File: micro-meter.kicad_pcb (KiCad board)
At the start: 2 copper layers, 50 x 50 mm, 93 parts, among them J1 DC_IN, J10 5V_OUT, J11 LEDS_DATA, J2 SPI, J3 I2C / UART, J4 IN1, J5 IN2, J6 IN3, J7 IN4, J8 SWD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

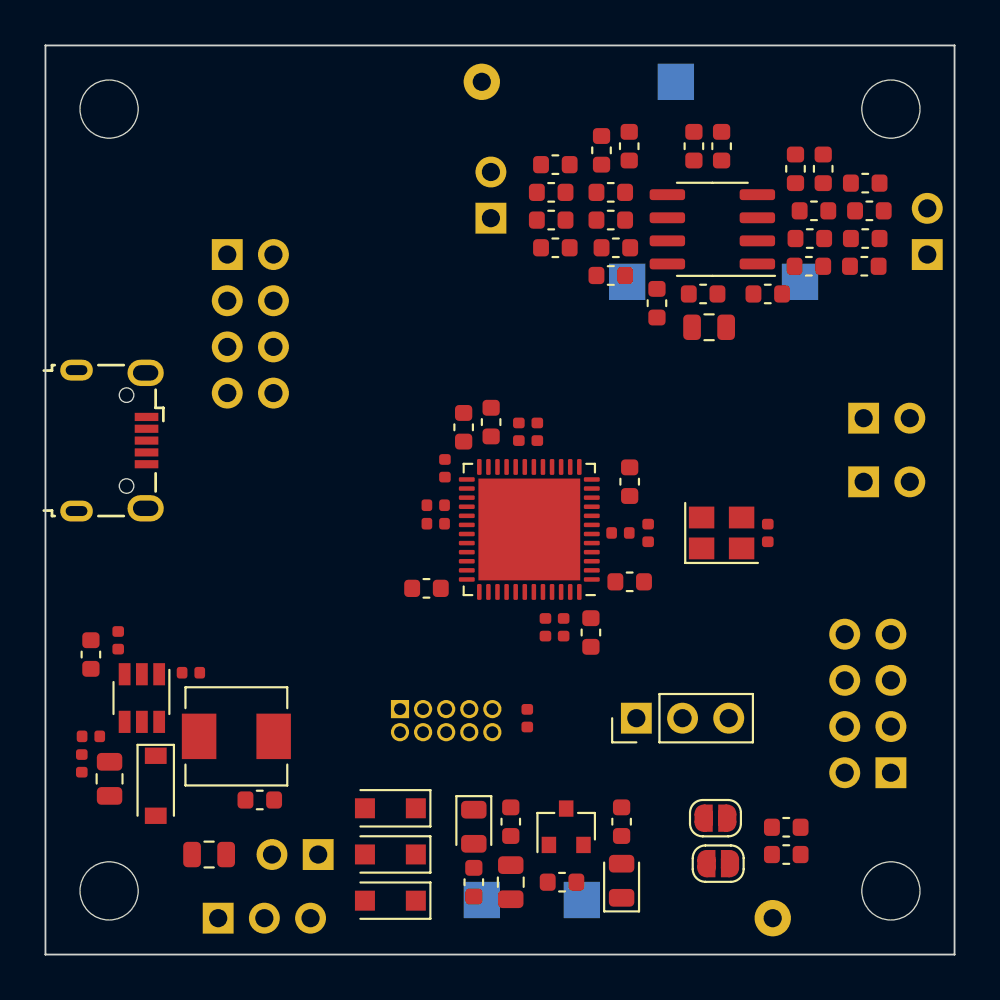
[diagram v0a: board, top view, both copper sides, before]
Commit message: Add inner layers and planes
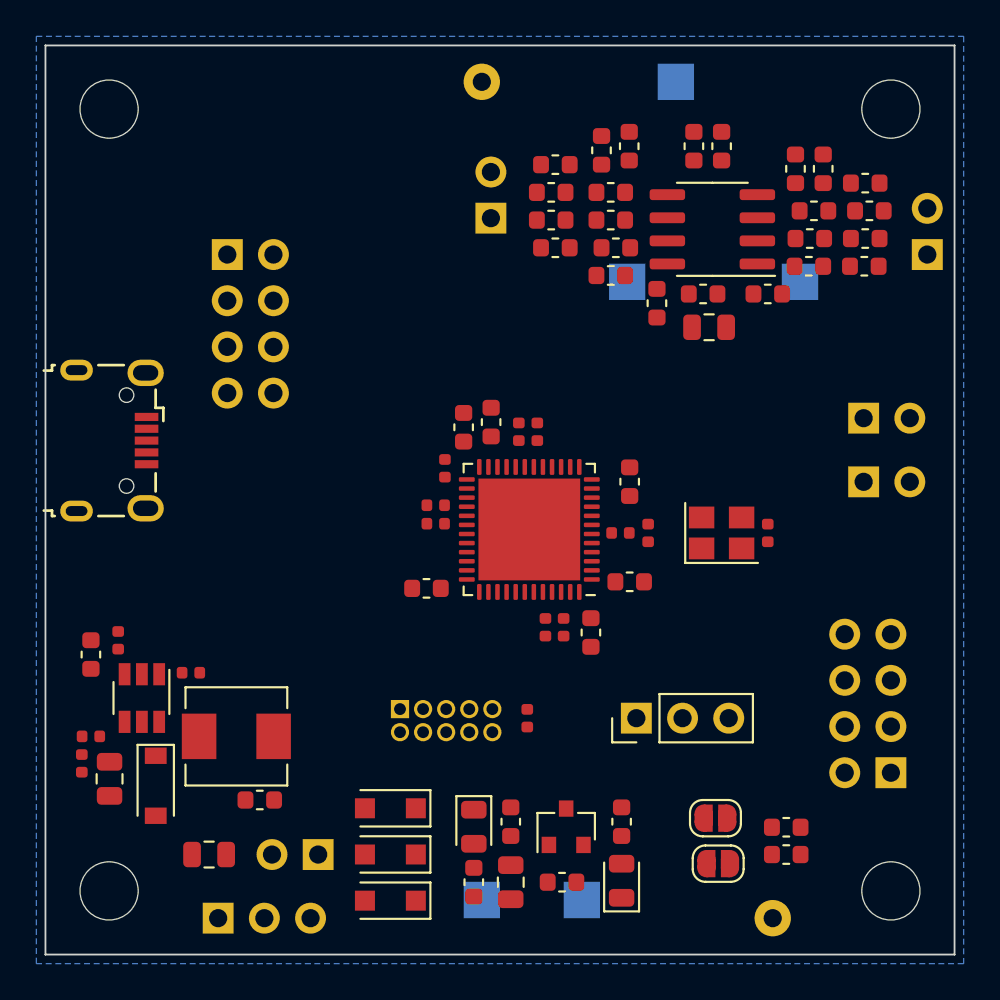
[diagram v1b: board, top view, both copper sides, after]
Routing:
- added copper zone on B.Cu, net +3V3
- added copper zone on In1.Cu, net GND
- added copper zone on In2.Cu, net GND
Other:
- copper layers 2 -> 4
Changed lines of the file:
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@@
   (layers
     (0 F.Cu signal)
+    (1 In1.Cu power)
+    (2 In2.Cu power)
     (31 B.Cu signal)
     (32 B.Adhes user)
@@
   (gr_line (start 70 170) (end 70 120) (layer Edge.Cuts) (width 0.1))
   (gr_line (start 120 170) (end 70 170) (layer Edge.Cuts) (width 0.1))
+  (zone (net 2) (net_name GND) (layer In1.Cu) (hatch edge 0.508)
+    (connect_pads (clearance 0.508))
+    (min_thickness 0.254)
+    (fill yes (arc_segments 32) (thermal_gap 0.508) (thermal_bridge_width 0.508))
+    (polygon
+      (pts
+        (xy 120.5 170.5) (xy 69.5 170.5) (xy 69.5 119.5) (xy 120.5 119.5)
+      )
+    )
+  )
+  (zone (net 2) (net_name GND) (layer In2.Cu) (hatch edge 0.508)
+    (connect_pads (clearance 0.508))
+    (min_thickness 0.254)
+    (fill yes (arc_segments 32) (thermal_gap 0.508) (thermal_bridge_width 0.508))
+    (polygon
+      (pts
+        (xy 120.5 170.5) (xy 69.5 170.5) (xy 69.5 119.5) (xy 120.5 119.5)
+      )
+    )
+  )
+  (zone (net 4) (net_name +3V3) (layer B.Cu) (hatch edge 0.508)
+    (connect_pads (clearance 0.508))
+    (min_thickness 0.254)
+    (fill yes (arc_segments 32) (thermal_gap 0.508) (thermal_bridge_width 0.508))
+    (polygon
+      (pts
+        (xy 120.5 170.5) (xy 69.5 170.5) (xy 69.5 119.5) (xy 120.5 119.5)
+      )
+    )
+  )
 )

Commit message: Add rounded corners
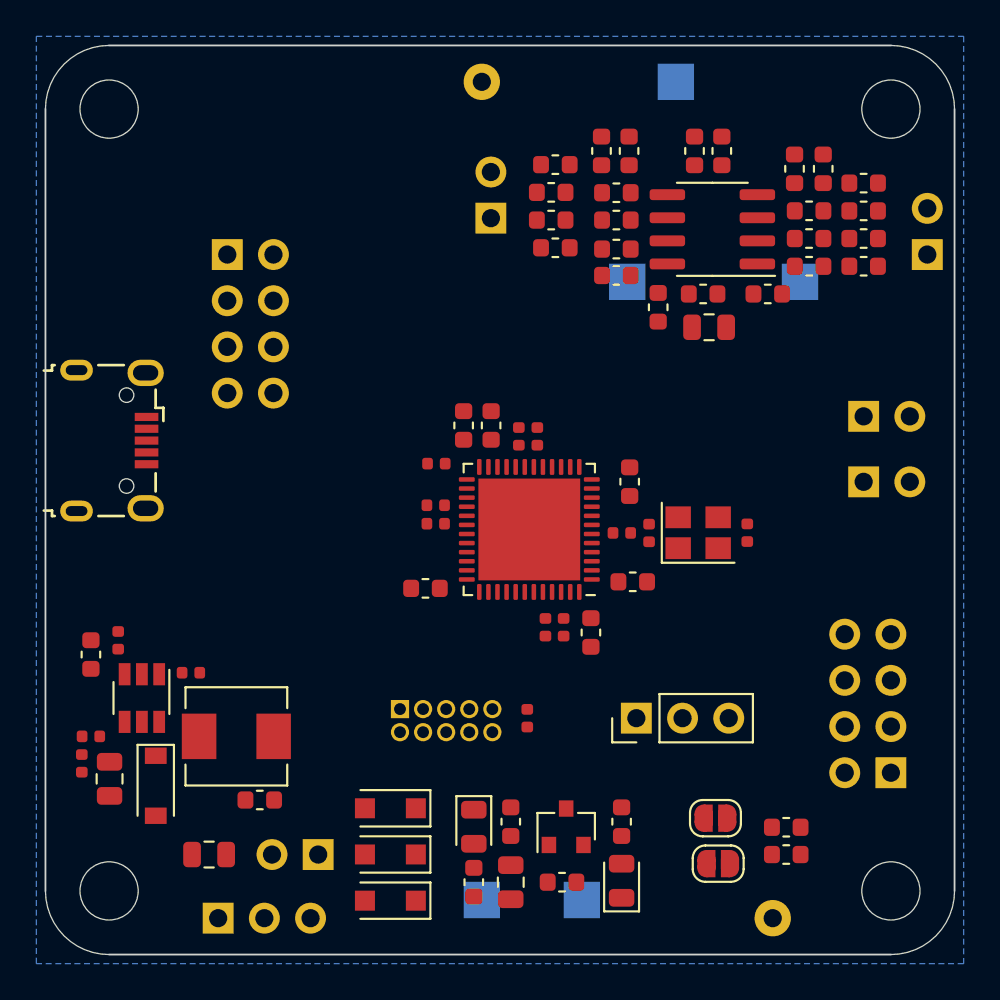
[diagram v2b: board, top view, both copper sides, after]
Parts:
- moved Y1 1.29 mm to (105.9, 146.8)
- moved C1 1.13 mm to (108.6, 146.8)
- moved R7 0.54 mm to (91.5, 143.0), turned to 0 degrees
- moved R18 0.32 mm to (115.0, 129.1)
- moved R29 0.31 mm to (101.4, 128.1)
- moved R27 0.31 mm to (101.4, 132.7)
- moved R28 0.31 mm to (101.4, 129.6)
- moved R26 0.27 mm to (112.0, 129.1)
- moved R31 0.26 mm to (105.7, 125.8)
- moved C34 0.26 mm to (107.2, 125.8)
- moved C29 0.26 mm to (102.1, 125.8)
- moved R12 0.25 mm to (97.1, 141.5)
- moved R6 0.25 mm to (96.0, 141.5)
- moved C37 0.23 mm to (103.7, 134.4)
- moved C4 0.18 mm to (94.5, 140.9)
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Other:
- outline, holes or cut-outs redrawn
- rule trace_min: 0.2 -> 0.127
- rule via_min_drill: 0.3 -> 0.2
- rule via_min_size: 0.4 -> 0.45

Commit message: Add design rules and default track/via sizes
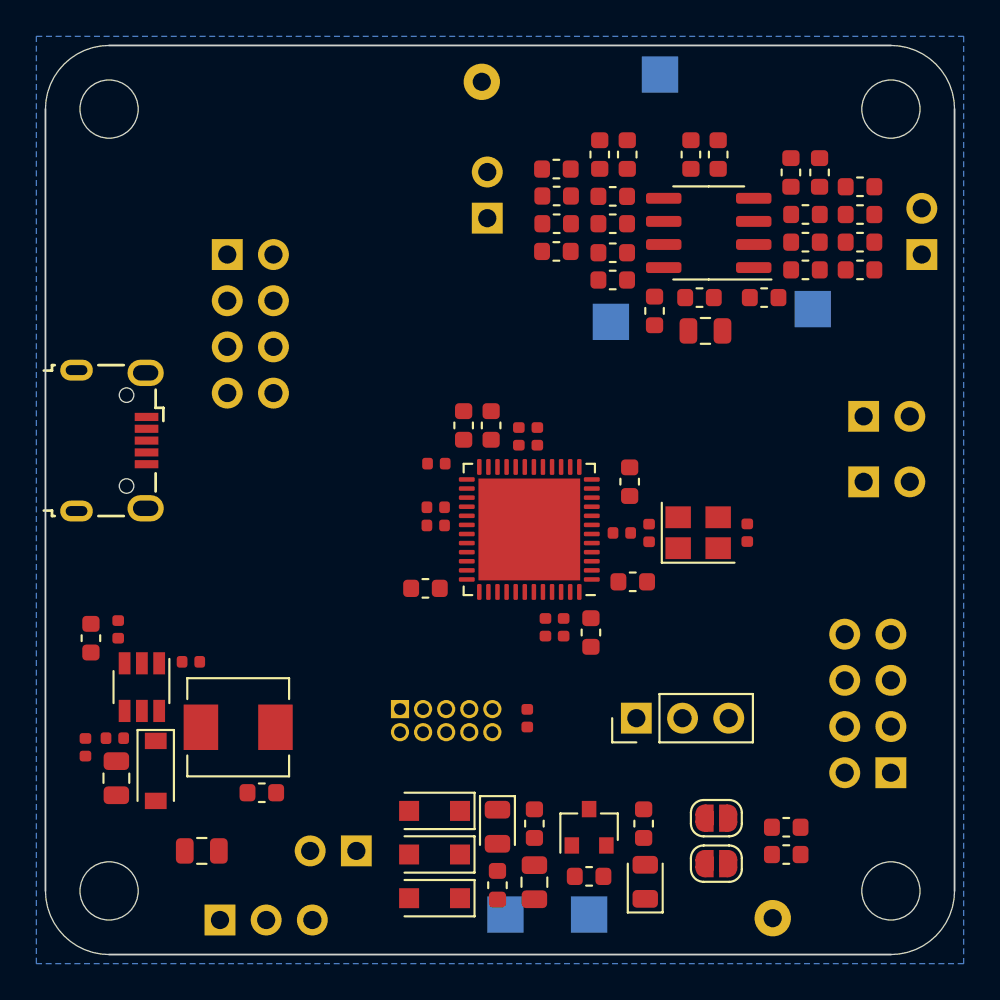
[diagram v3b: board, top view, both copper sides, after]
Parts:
- moved D30 2.43 mm to (91.4, 162.1)
- moved D5 2.43 mm to (91.4, 166.9)
- moved D4 2.43 mm to (91.4, 164.5)
- moved TP7 2.38 mm to (101.1, 135.2)
- moved J10 2.11 mm to (87.1, 164.3)
- moved TP6 1.66 mm to (112.2, 134.5)
- moved TP10 1.53 mm to (95.3, 167.8)
- moved C19 1.52 mm to (99.9, 165.7)
- moved R2 1.32 mm to (73.8, 158.1)
- moved R14 1.31 mm to (94.9, 166.2)
- moved C16 1.30 mm to (96.9, 162.8)
- moved D13 1.30 mm to (103.0, 166.0)
- moved D6 1.30 mm to (94.9, 163.0)
- moved FB3 1.30 mm to (96.9, 166.0)
- moved U3 1.26 mm to (99.9, 163.0)
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
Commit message: Add routing
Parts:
- added J12: I2C, Connector_PinSocket_2.54mm:PinSocket_1x03_P2.54mm_Vertical, B.Cu at (107.2, 162.1)
- J3: value I2C / UART -> UART; footprint Connector_PinSocket_2.54mm:PinSocket_2x04_P2.54mm_Vertical -> Connector_PinSocket_2.54mm:PinSocket_1x03_P2.54mm_Vertical
- J4: value IN1 -> IN3
- J5: value IN2 -> IN4
- J6: value IN3 -> IN1
- J7: value IN4 -> IN2
- TP6: value TP_AIN0 -> TP_AIN2
- TP7: value TP_AIN1 -> TP_AIN3
- moved J3 36.5 mm to (83.1, 145.3)
- moved J11 15.7 mm to (118.0, 154.5), turned to 0 degrees
- moved FB2 11.5 mm to (111.8, 145.8), turned to 90 degrees
- moved J2 8.26 mm to (72.1, 129.1)
- moved JP2 6.87 mm to (110.3, 156.5), turned to 90 degrees
- moved C1 5.53 mm to (103.1, 146.2), turned to 270 degrees
- moved R15 4.08 mm to (110.5, 160.4), turned to 180 degrees
- moved R16 4.08 mm to (110.5, 158.9), turned to 180 degrees
- moved JP1 3.99 mm to (110.2, 162.8), turned to 270 degrees
- moved J7 3.96 mm to (117.9, 137.7), turned to 0 degrees
- moved TP8 3.69 mm to (100.2, 122.4)
- moved J9 3.27 mm to (73.8, 145.0)
- moved TP7 3.26 mm to (100.9, 131.9)
- moved TP6 3.02 mm to (111.5, 131.6)
- moved J6 2.91 mm to (117.9, 143.8), turned to 0 degrees
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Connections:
- C26 pad 2: AIN0 -> AIN2
- C28 pad 2: AIN1 -> AIN3
- J3 pad 1: I2C2_SCL -> USART1_RX
- J3 pad 2: +3V3 -> GND
- J3 pad 3: I2C2_SDA -> USART1_TX
- J6 pad 1: AIN2 -> AIN0
- J7 pad 1: AIN3 -> AIN1
- R24 pad 1: AIN0 -> AIN2
- R27 pad 1: AIN1 -> AIN3
- TP6 pad 1: AIN0 -> AIN2
- TP7 pad 1: AIN1 -> AIN3
- U4 pad 1: AIN0 -> AIN2
- U4 pad 7: AIN1 -> AIN3
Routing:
- net +3V3: track 0.00 -> 116.6 mm, vias 0 -> 10
- net GND: track 0.00 -> 56.7 mm, vias 0 -> 44
- net 5V_OUT: track 0.00 -> 35.3 mm, vias 0 -> 2
- net VDDA: track 0.00 -> 31.0 mm, vias 0 -> 2
- net VBUS: track 0.00 -> 30.2 mm
- net CE+I2S2_MCK: track 0.00 -> 30.1 mm, vias 0 -> 1
- net SPI2_SCK: track 0.00 -> 27.4 mm, vias 0 -> 1
- net +5V: track 0.00 -> 27.3 mm, vias 0 -> 1
- net SPI2_CIPO: track 0.00 -> 25.0 mm, vias 0 -> 1
- net I2C1_SCL: track 0.00 -> 22.9 mm
- net SPI2_COPI: track 0.00 -> 22.2 mm
- net IRQ: track 0.00 -> 21.9 mm, vias 0 -> 1
- net VAA: track 0.00 -> 21.6 mm
- net ~SPI2_CS: track 0.00 -> 21.4 mm
- net AIN1: track 0.00 -> 21.2 mm
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- removed copper zone on B.Cu, net +3V3

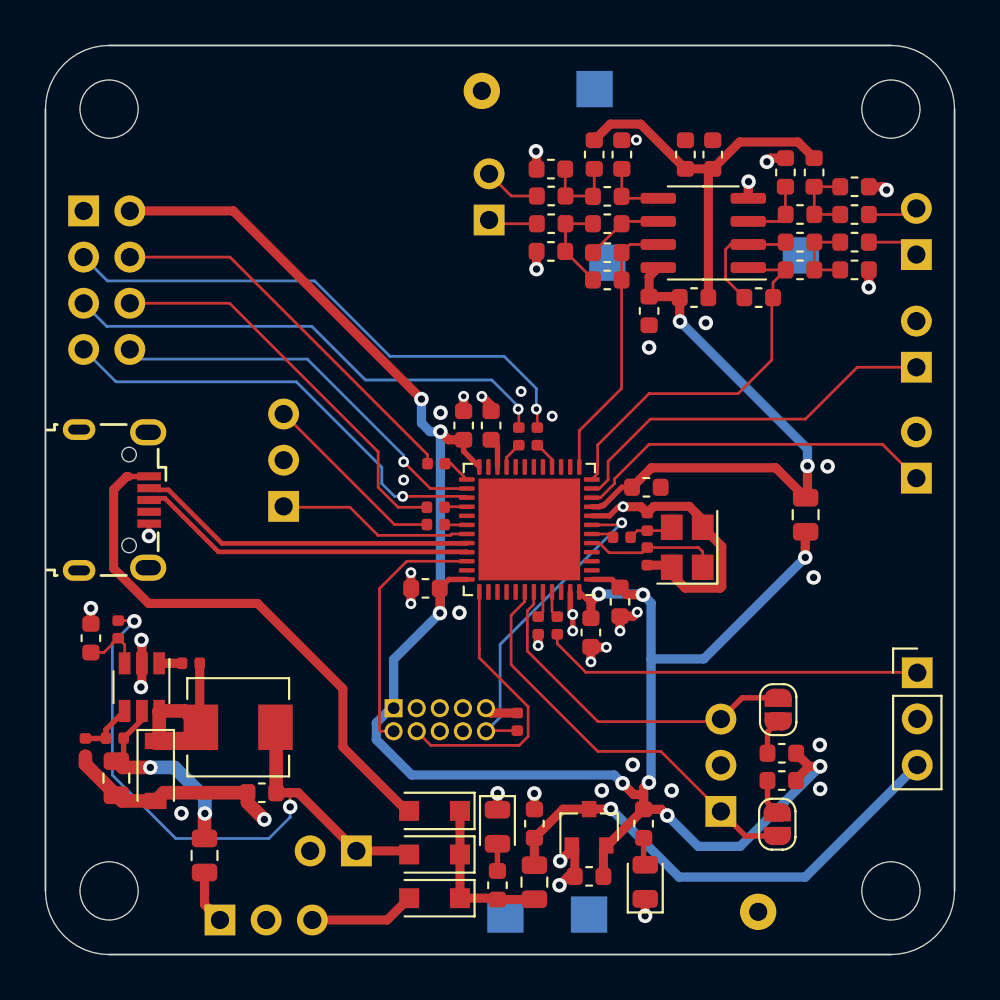
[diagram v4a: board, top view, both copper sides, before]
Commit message: Cleanup routing
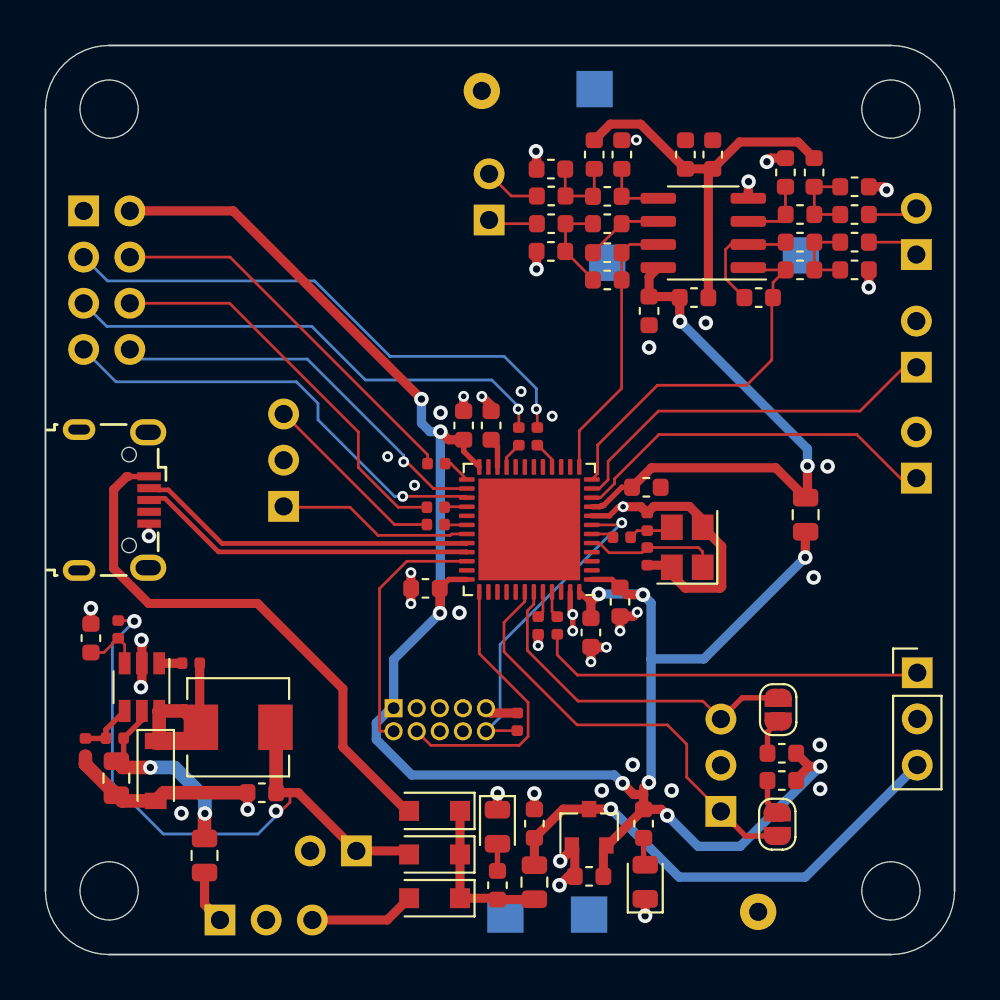
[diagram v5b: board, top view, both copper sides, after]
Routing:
- net I2C1_SCL: track 22.9 -> 24.1 mm
- net GND: track 56.7 -> 55.8 mm, vias 44 -> 45

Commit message: Cleanup routing
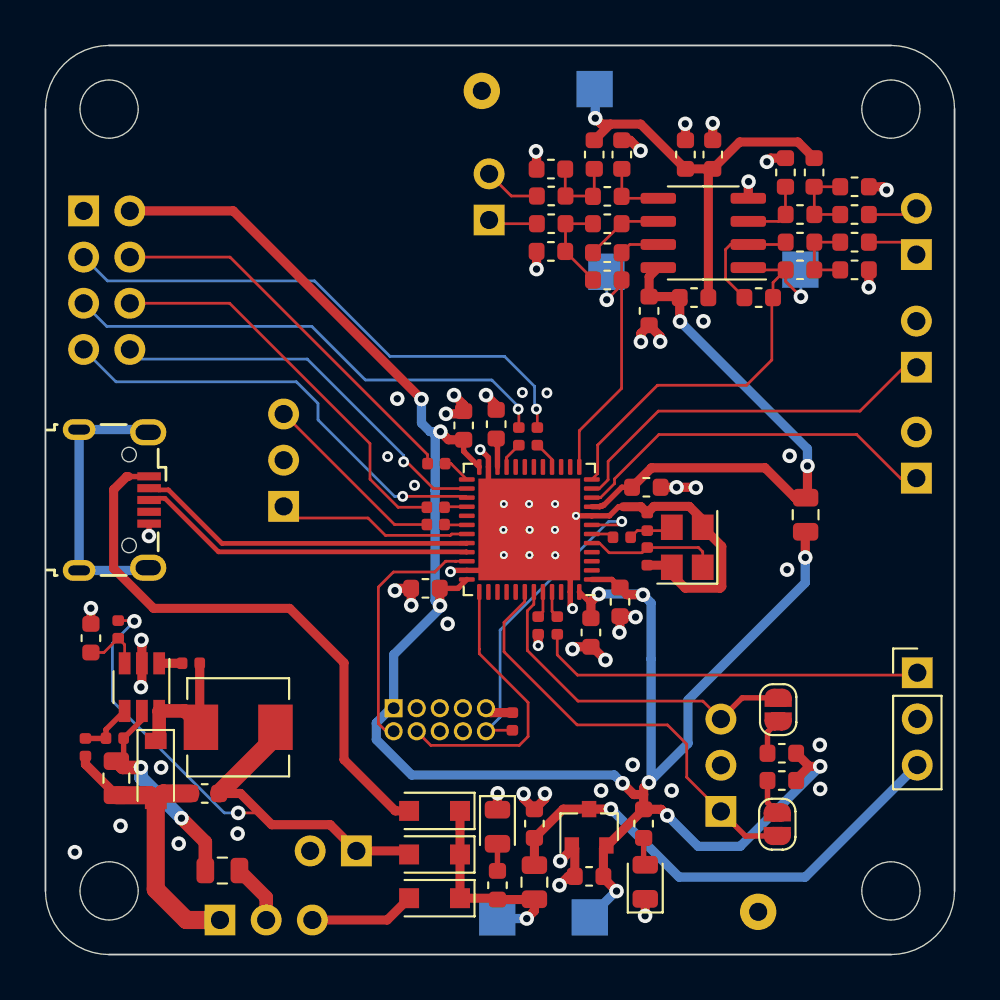
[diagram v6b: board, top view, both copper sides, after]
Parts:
- moved C7 3.14 mm to (78.8, 161.1)
- moved FB1 1.28 mm to (79.7, 165.4), turned to 180 degrees
- moved TP6 0.78 mm to (111.5, 132.3)
- moved TP7 0.50 mm to (100.8, 132.4)
- moved TP10 0.48 mm to (94.8, 168.0)
- moved C4 0.29 mm to (94.8, 140.8)
- moved C46 0.27 mm to (95.7, 157.2)
- moved TP4 0.16 mm to (99.9, 168.0)
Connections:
- J1 pad 1: Net-(FB1-Pad1) -> GND
- J1 pad 2: GND -> Net-(FB1-Pad1)
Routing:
- net GND: track 55.8 -> 75.1 mm, vias 45 -> 65
- net Net-(J9-Pad6): track 0.00 -> 15.5 mm
- net +3V3: track 116.6 -> 124.8 mm, vias 10 -> 11
- net AIN2: track 21.1 -> 24.7 mm, vias 0 -> 1
- net AIN3: track 15.0 -> 18.2 mm, vias 0 -> 1
- net Net-(D30-Pad1): track 8.93 -> 11.8 mm, vias 0 -> 1
- net Net-(C5-Pad1): track 10.7 -> 7.94 mm
- net VAA: track 21.6 -> 24.3 mm, vias 0 -> 1
- net VBUS: track 30.2 -> 31.5 mm
- net Net-(C3-Pad1): track 11.3 -> 12.0 mm
